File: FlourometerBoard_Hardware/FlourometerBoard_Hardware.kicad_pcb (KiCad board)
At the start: 2 copper layers, 105.7 x 36.6 mm, 15 parts, among them J1 RJ45_LED_Shielded, U1 Teensy4.1_DEV-16771, U3 OKI

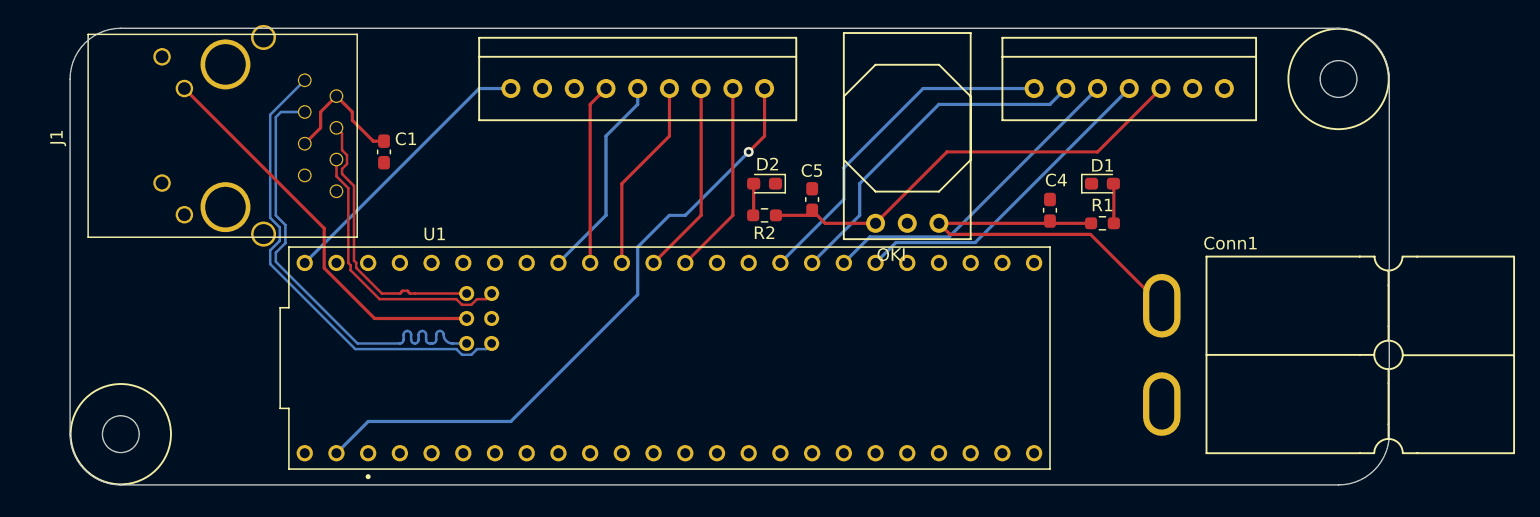
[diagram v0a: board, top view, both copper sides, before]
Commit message: Added Pull Down Resistors to MOSFETs
And some other things
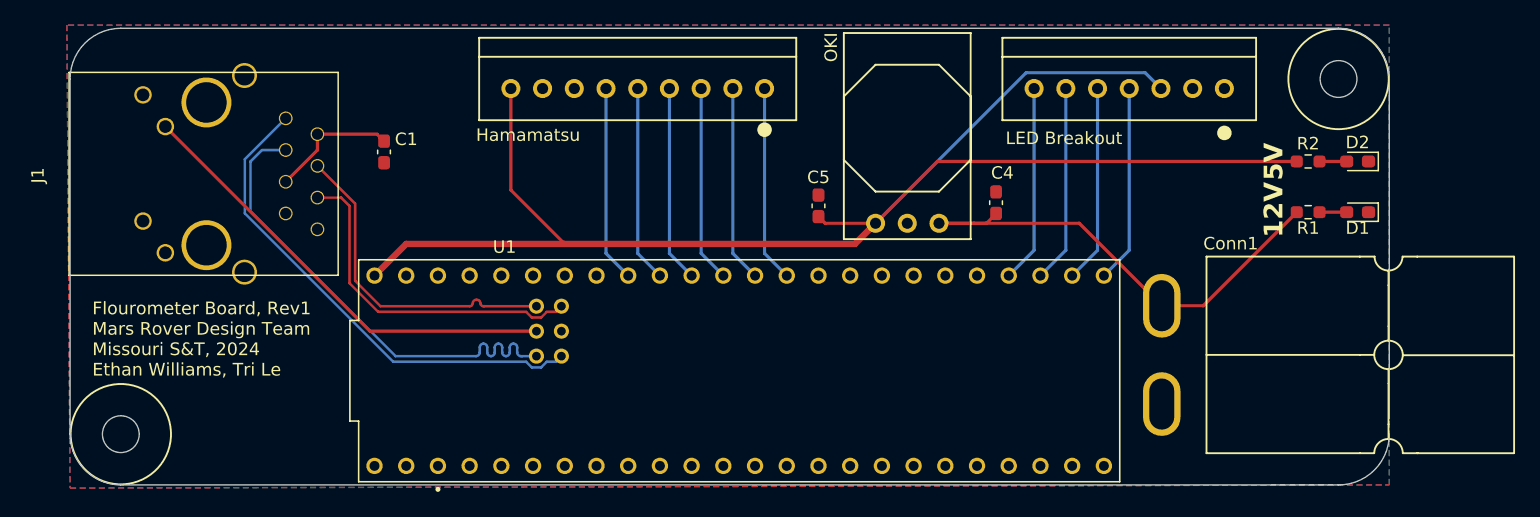
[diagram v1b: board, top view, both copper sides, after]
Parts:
- moved D2 47.5 mm to (141.5, 92.2)
- moved R2 43.8 mm to (137.5, 92.2), turned to 0 degrees
- moved D1 20.6 mm to (141.5, 96.3), turned to 180 degrees
- moved R1 16.5 mm to (137.5, 96.3)
- moved U1 5.68 mm to (91.9, 109.0)
- moved C4 4.36 mm to (112.5, 95.5)
- moved J1 3.41 mm to (36.3, 93.3)
- moved C5 0.72 mm to (98.3, 95.8)
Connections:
- U1 pad 0: WHITE_LED -> unconnected-(U1-RX1-Pad0)
- U1 pad 13: unconnected-(U1-SCK-Pad13) -> WHITE_LED
- U1 pad 17: EOS -> TRG
- U1 pad 18: TRG -> EOS
- U1 pad 33: unconnected-(U1-MCLK2-Pad33) -> 400nm LED
- U1 pad 34: unconnected-(U1-RX8-Pad34) -> 430nm LED
- U1 pad 35: unconnected-(U1-TX8-Pad35) -> 522nm LED
- U1 pad 36: unconnected-(U1-CS2-Pad36) -> 530nm LED
- U1 pad 38: 400nm LED -> unconnected-(U1-A14-Pad38)
- U1 pad 39: 430nm LED -> unconnected-(U1-A15-Pad39)
- U1 pad 40: 522nm LED -> unconnected-(U1-A16-Pad40)
- U1 pad 41: 530nm LED -> unconnected-(U1-A17-Pad41)
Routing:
- net +5V: track 58.2 -> 125.1 mm
- net WHITE_LED: track 50.9 -> 15.7 mm, vias 1 -> 0
- net 530nm LED: track 27.6 -> 15.8 mm
- net 522nm LED: track 27.6 -> 15.8 mm
- net 430nm LED: track 26.1 -> 15.8 mm
- net 400nm LED: track 26.1 -> 15.8 mm
- net +12V: track 32.9 -> 39.4 mm
- net R-: track 22.1 -> 27.5 mm
- net LED: track 32.1 -> 36.5 mm
- net R+: track 22.1 -> 26.4 mm
- net T-: track 36.8 -> 39.2 mm
- net T+: track 37.6 -> 39.8 mm
- net EOS: track 14.5 -> 15.7 mm
- net Net-(D1-A): track 3.19 -> 2.17 mm
- net TRG: track 16.6 -> 15.7 mm
- added copper zone on B.Cu, net GND
- added copper zone on F.Cu, net GND
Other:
- outline, holes or cut-outs redrawn
- board text added: "12V"
- board text added: "5V"
- board text added: "Flourometer Board, Rev1 Mars Rover Design Team Missouri S&T, 2024 Ethan Williams, Tri Le"
- board text added: "Hamamatsu"
- board text added: "LED Breakout"

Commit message: Complied with most of CDR changes
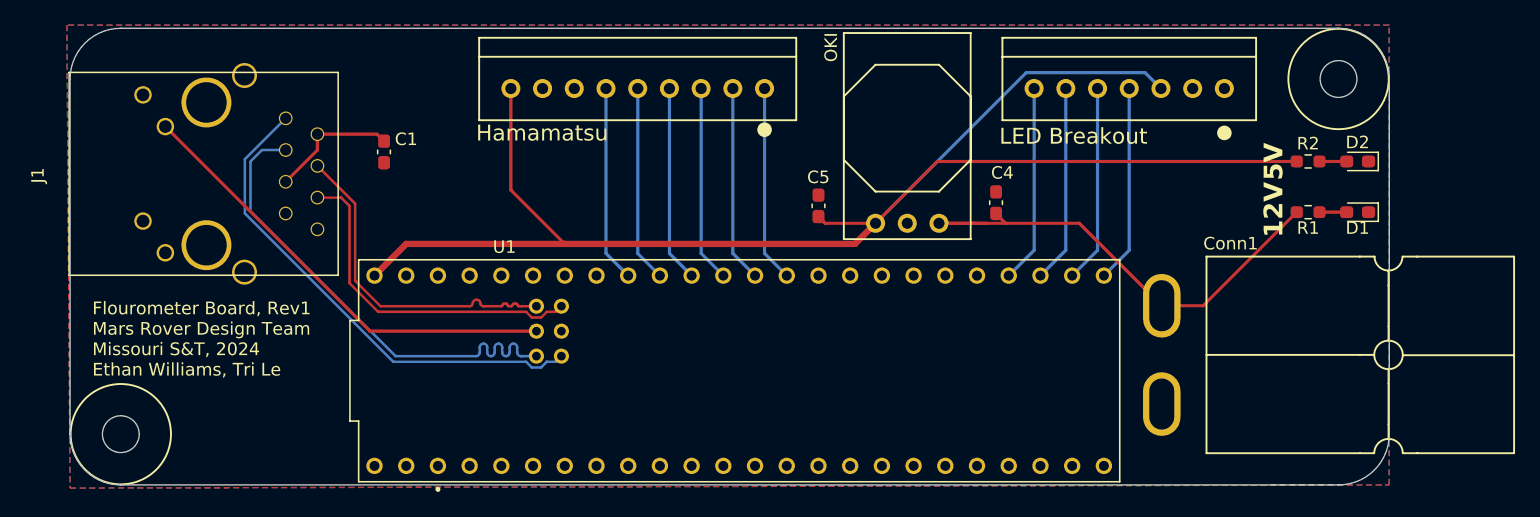
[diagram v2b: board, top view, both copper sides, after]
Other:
- outline, holes or cut-outs redrawn
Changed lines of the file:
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@@
   (gr_arc (start 139.954 81.534) (mid 142.827682 82.724318) (end 144.018 85.598)
     (stroke (width 0.1) (type default)) (layer "Edge.Cuts"))
-  (gr_line (start 144.018 85.598) (end 144.018 112.776)
+  (gr_line (start 144.018 85.598) (end 144.018 114.046)
     (stroke (width 0.1) (type default)) (layer "Edge.Cuts"))
   (gr_line (start 42.418 118.11) (end 139.954 118.11)
@@
   )
   (gr_text "Hamamatsu" (at 70.866 90.678) (layer "F.SilkS")
-    (effects (font (size 1 1) (thickness 0.15)) (justify left bottom))
+    (effects (font (size 1.27 1.27) (thickness 0.15)) (justify left bottom))
   )
-  (gr_text "LED Breakout" (at 113.284 90.932) (layer "F.SilkS")
-    (effects (font (size 1 1) (thickness 0.15)) (justify left bottom))
+  (gr_text "LED Breakout" (at 112.776 90.932) (layer "F.SilkS")
+    (effects (font (size 1.27 1.27) (thickness 0.15)) (justify left bottom))
   )
   (gr_text "5V" (at 135.636 93.726 90) (layer "F.SilkS")
@@
   (segment (start 63.5 90.5775) (end 62.9405 90.018) (width 0.254) (layer "F.Cu") (net 2))
   (segment (start 58.166 91.288) (end 55.626 93.828) (width 0.254) (layer "F.Cu") (net 2))
+  (segment (start 136.605 96.266) (end 129.112 103.759) (width 0.254) (layer "F.Cu") (net 3))
+  (segment (start 113.284 97.155) (end 119.1908 97.155) (width 0.254) (layer "F.Cu") (net 3))
+  (segment (start 111.76 97.155) (end 110.744 97.155) (width 0.254) (layer "F.Cu") (net 3))
+  (segment (start 112.522 96.393) (end 113.284 97.155) (width 0.254) (layer "F.Cu") (net 3))
   (segment (start 112.522 96.3665) (end 112.522 96.393) (width 0.254) (layer "F.Cu") (net 3))
-  (segment (start 112.522 96.393) (end 111.76 97.155) (width 0.254) (layer "F.Cu") (net 3))
-  (segment (start 136.605 96.266) (end 129.112 103.759) (width 0.254) (layer "F.Cu") (net 3))
-  (segment (start 107.95 97.155) (end 119.1908 97.155) (width 0.254) (layer "F.Cu") (net 3))
-  (segment (start 111.76 97.155) (end 110.744 97.155) (width 0.254) (layer "F.Cu") (net 3))
+  (segment (start 107.95 97.155) (end 113.284 97.155) (width 0.254) (layer "F.Cu") (net 3))
   (segment (start 129.112 103.759) (end 125.7948 103.759) (width 0.254) (layer "F.Cu") (net 3))
   (segment (start 119.1908 97.155) (end 125.7948 103.759) (width 0.254) (layer "F.Cu") (net 3))
@@
   (arc (start 72.966 107.496) (mid 73.053868 107.708132) (end 73.266 107.796) (width 0.2) (layer "B.Cu") (net 17))
   (arc (start 71.766 107.496) (mid 71.853868 107.708132) (end 72.066 107.796) (width 0.2) (layer "B.Cu") (net 17))
+  (segment (start 61.185 101.7608) (end 63.2202 103.796) (width 0.2) (layer "F.Cu") (net 19))
   (segment (start 61.185 95.577) (end 61.185 101.7608) (width 0.2) (layer "F.Cu") (net 19))
+  (segment (start 74.498 103.796) (end 75.708 103.796) (width 0.2) (layer "F.Cu") (net 19))
+  (segment (start 71.558 103.796) (end 72.898 103.796) (width 0.2) (layer "F.Cu") (net 19))
+  (segment (start 74.298 103.796) (end 74.498 103.796) (width 0.2) (layer "F.Cu") (net 19))
   (segment (start 63.2202 103.796) (end 70.358 103.796) (width 0.2) (layer "F.Cu") (net 19))
-  (segment (start 61.185 101.7608) (end 63.2202 103.796) (width 0.2) (layer "F.Cu") (net 19))
+  (segment (start 58.166 92.558) (end 61.185 95.577) (width 0.2) (layer "F.Cu") (net 19))
+  (segment (start 73.898 103.596) (end 74.098 103.596) (width 0.2) (layer "F.Cu") (net 19))
+  (segment (start 71.466 103.796) (end 71.558 103.796) (width 0.2) (layer "F.Cu") (net 19))
+  (segment (start 73.498 103.796) (end 73.698 103.796) (width 0.2) (layer "F.Cu") (net 19))
   (segment (start 70.866 103.288) (end 70.958 103.288) (width 0.2) (layer "F.Cu") (net 19))
-  (segment (start 71.466 103.796) (end 71.558 103.796) (width 0.2) (layer "F.Cu") (net 19))
-  (segment (start 58.166 92.558) (end 61.185 95.577) (width 0.2) (layer "F.Cu") (net 19))
-  (segment (start 71.558 103.796) (end 75.708 103.796) (width 0.2) (layer "F.Cu") (net 19))
+  (segment (start 73.098 103.596) (end 73.298 103.596) (width 0.2) (layer "F.Cu") (net 19))
+  (arc (start 73.798 103.696) (mid 73.827289 103.625289) (end 73.898 103.596) (width 0.2) (layer "F.Cu") (net 19))
+  (arc (start 73.298 103.596) (mid 73.368711 103.625289) (end 73.398 103.696) (width 0.2) (layer "F.Cu") (net 19))
+  (arc (start 73.398 103.696) (mid 73.427289 103.766711) (end 73.498 103.796) (width 0.2) (layer "F.Cu") (net 19))
+  (arc (start 70.358 103.796) (mid 70.537605 103.721605) (end 70.612 103.542) (width 0.2) (layer "F.Cu") (net 19))
+  (arc (start 74.198 103.696) (mid 74.227289 103.766711) (end 74.298 103.796) (width 0.2) (layer "F.Cu") (net 19))
   (arc (start 71.212 103.542) (mid 71.286395 103.721605) (end 71.466 103.796) (width 0.2) (layer "F.Cu") (net 19))
+  (arc (start 74.098 103.596) (mid 74.168711 103.625289) (end 74.198 103.696) (width 0.2) (layer "F.Cu") (net 19))
+  (arc (start 70.612 103.542) (mid 70.686395 103.362395) (end 70.866 103.288) (width 0.2) (layer "F.Cu") (net 19))
+  (arc (start 73.698 103.796) (mid 73.768711 103.766711) (end 73.798 103.696) (width 0.2) (layer "F.Cu") (net 19))
   (arc (start 70.958 103.288) (mid 71.137605 103.362395) (end 71.212 103.542) (width 0.2) (layer "F.Cu") (net 19))
-  (arc (start 70.612 103.542) (mid 70.686395 103.362395) (end 70.866 103.288) (width 0.2) (layer "F.Cu") (net 19))
-  (arc (start 70.358 103.796) (mid 70.537605 103.721605) (end 70.612 103.542) (width 0.2) (layer "F.Cu") (net 19))
+  (arc (start 72.998 103.696) (mid 73.027289 103.625289) (end 73.098 103.596) (width 0.2) (layer "F.Cu") (net 19))
+  (arc (start 72.898 103.796) (mid 72.968711 103.766711) (end 72.998 103.696) (width 0.2) (layer "F.Cu") (net 19))
   (segment (start 58.166 95.098) (end 60.069603 95.098) (width 0.2) (layer "F.Cu") (net 20))
   (segment (start 60.069603 95.098) (end 60.735 95.763397) (width 0.2) (layer "F.Cu") (net 20))

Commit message: Finished Main Board Secondary Notes
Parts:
- moved REF** 3.41 mm to (43.9, 111.0)
- moved REF** 0.76 mm to (139.2, 85.6)
- moved D1 0.26 mm to (141.5, 96.0)
- moved R1 0.26 mm to (137.6, 96.0)
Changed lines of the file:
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@@
   )
   (footprint "Resistor_SMD:R_0603_1608Metric_Pad0.98x0.95mm_HandSolder" (layer "F.Cu")
-    (at 137.5175 96.266)
+    (at 137.5645 96.012)
     (descr "Resistor SMD 0603 (1608 Metric), square (rectangular) end terminal, IPC_7351 nominal with elongated pad for handsoldering. (Body size source: IPC-SM-782 page 72, https://www.pcb-3d.com/wordpress/wp-content/uploads/ipc-sm-782a_amendment_1_and_2.pdf), generated with kicad-footprint-generator")
     (tags "resistor handsolder")
@@
   )
   (footprint "LED_SMD:LED_0603_1608Metric_Pad1.05x0.95mm_HandSolder" (layer "F.Cu")
-    (at 141.478 96.266 180)
+    (at 141.525 96.012 180)
     (descr "LED SMD 0603 (1608 Metric), square (rectangular) end terminal, IPC_7351 nominal, (Body size source: http://www.tortai-tech.com/upload/download/2011102023233369053.pdf), generated with kicad-footprint-generator")
     (tags "LED handsolder")
@@
     (property "Sheetname" "")
     (attr through_hole)
-    (fp_text reference "U1" (at -18.796 -9.906) (layer "F.SilkS")
+    (fp_text reference "U1" (at -24.13 -9.906) (layer "F.SilkS")
         (effects (font (size 1 1) (thickness 0.15)))
     )
@@
   )
   (footprint "MRDT_Drill_Holes:4_40_Hole" (layer "F.Cu")
-    (at 139.954 85.598)
+    (at 139.192 85.598)
     (clearance 2.54)
     (attr through_hole)
@@
   )
   (footprint "MRDT_Drill_Holes:4_40_Hole" (layer "F.Cu")
-    (at 42.418 114.046)
+    (at 43.942 110.998)
     (clearance 2.54)
     (attr through_hole)
@@
   (gr_line (start 139.954 81.534) (end 42.418 81.534)
     (stroke (width 0.1) (type default)) (layer "Edge.Cuts"))
-  (gr_text "Flourometer Board, Rev1\nMars Rover Design Team\nMissouri S&T, 2024\nEthan Williams, Tri Le" (at 40.132 109.474) (layer "F.SilkS")
+  (gr_text "Flourometer Board, Rev1\nMars Rover Design Team\nMissouri S&T, 2024\nEthan Williams, Tri Le" (at 70.866 99.568) (layer "F.SilkS")
     (effects (font (size 1.016 1.016) (thickness 0.2032)) (justify left bottom))
   )
@@
     (effects (font (size 1.27 1.27) (thickness 0.15)) (justify left bottom))
   )
-  (gr_text "5V" (at 135.636 93.726 90) (layer "F.SilkS")
+  (gr_text "5V" (at 135.636 92.964 90) (layer "F.SilkS")
     (effects (font (size 1.5 1.5) (thickness 0.3) bold) (justify left bottom))
   )
-  (gr_text "12V" (at 135.636 98.298 90) (layer "F.SilkS")
+  (gr_text "12V" (at 135.683 98.806 90) (layer "F.SilkS")
     (effects (font (size 1.5 1.5) (thickness 0.3) bold) (justify left bottom))
   )
@@
   (segment (start 93.98 99.568) (end 95.758 101.346) (width 0.254) (layer "B.Cu") (net 10))
   (segment (start 93.98 86.36) (end 93.98 99.568) (width 0.254) (layer "B.Cu") (net 10))
-  (segment (start 140.603 96.266) (end 138.43 96.266) (width 0.254) (layer "F.Cu") (net 11))
+  (segment (start 140.65 96.012) (end 138.477 96.012) (width 0.254) (layer "F.Cu") (net 11))
   (segment (start 140.603 92.202) (end 138.43 92.202) (width 0.254) (layer "F.Cu") (net 12))
   (segment (start 62.374 105.796) (end 45.986 89.408) (width 0.254) (layer "F.Cu") (net 14))
@@
     )
   )
-  (group "" (id 90442086-63db-422e-ab7e-9312ec5d8746)
-    (members
-      11e8780d-993f-42d5-9acd-4b932ebde27c
-      40cb9b00-6868-40f7-8a53-0b11d775f973
-      518d8b0e-db5b-41a8-9eec-7e50b72dadda
-      dde1ef96-f0de-43fa-830a-75287fb48a88
-    )
-  )
-  (group "" (id e3e4b9d9-a2f1-47d6-beaf-cf34f9fac8b5)
-    (members
-      2645f917-ace7-4194-9af5-7f0ed2e4def7
-      2b7fc009-49dc-4143-ba88-ab95a4cb0ede
-      d06abe1d-7b60-47e9-a06a-d4116a321863
-      e18c198a-0a47-4735-8d0a-c7b3510ddf32
-    )
-  )

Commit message: Final Revisions
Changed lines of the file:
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@@
     (property "ki_keywords" "cap capacitor")
     (attr smd)
-    (fp_text reference "C1" (at 1.016 1.778 180) (layer "F.SilkS")
+    (fp_text reference "C1" (at -2.54 2.413 180) (layer "F.SilkS")
         (effects (font (size 1 1) (thickness 0.15)))
     )

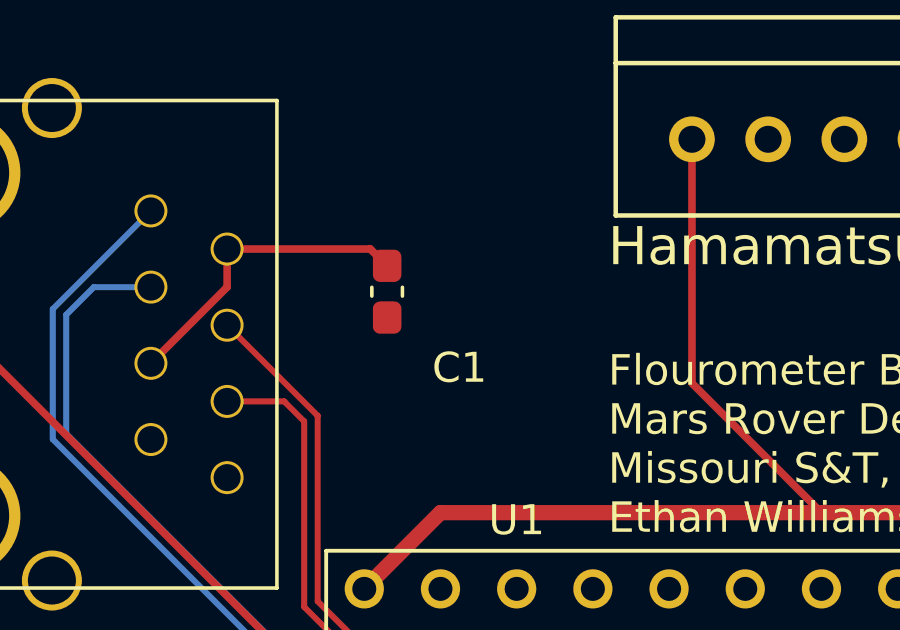
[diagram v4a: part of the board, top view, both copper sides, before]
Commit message: Revert "Final Revisions"
This reverts commit 08823e9a4bc57385ed17316fa6c40b2b69caaa08.
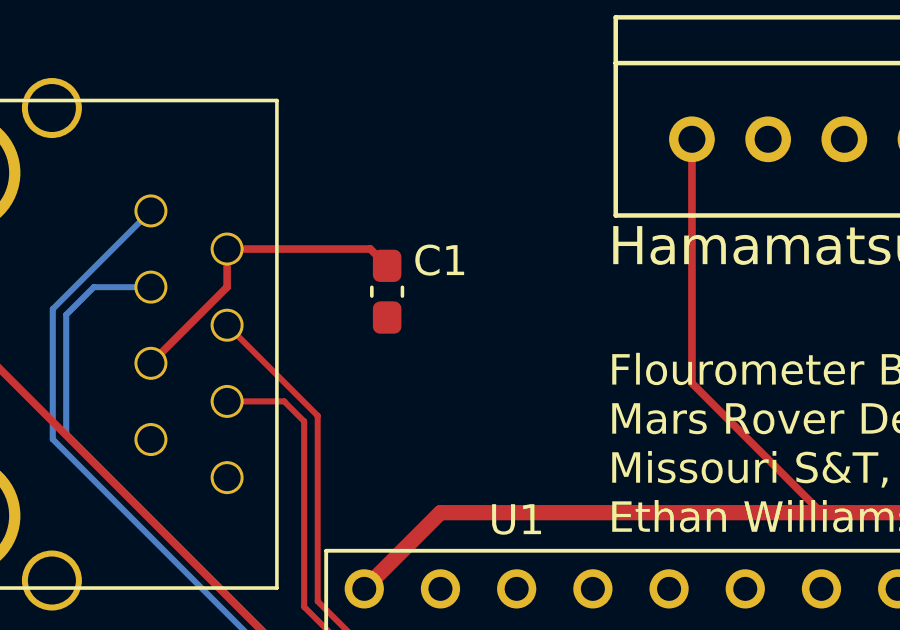
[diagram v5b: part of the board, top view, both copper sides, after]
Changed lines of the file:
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@@
     (property "ki_keywords" "cap capacitor")
     (attr smd)
-    (fp_text reference "C1" (at -2.54 2.413 180) (layer "F.SilkS")
+    (fp_text reference "C1" (at 1.016 1.778 180) (layer "F.SilkS")
         (effects (font (size 1 1) (thickness 0.15)))
     )
